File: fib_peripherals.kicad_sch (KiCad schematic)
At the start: 2 parts, among them J1 Raspi_Header, J2 Raspi_Header

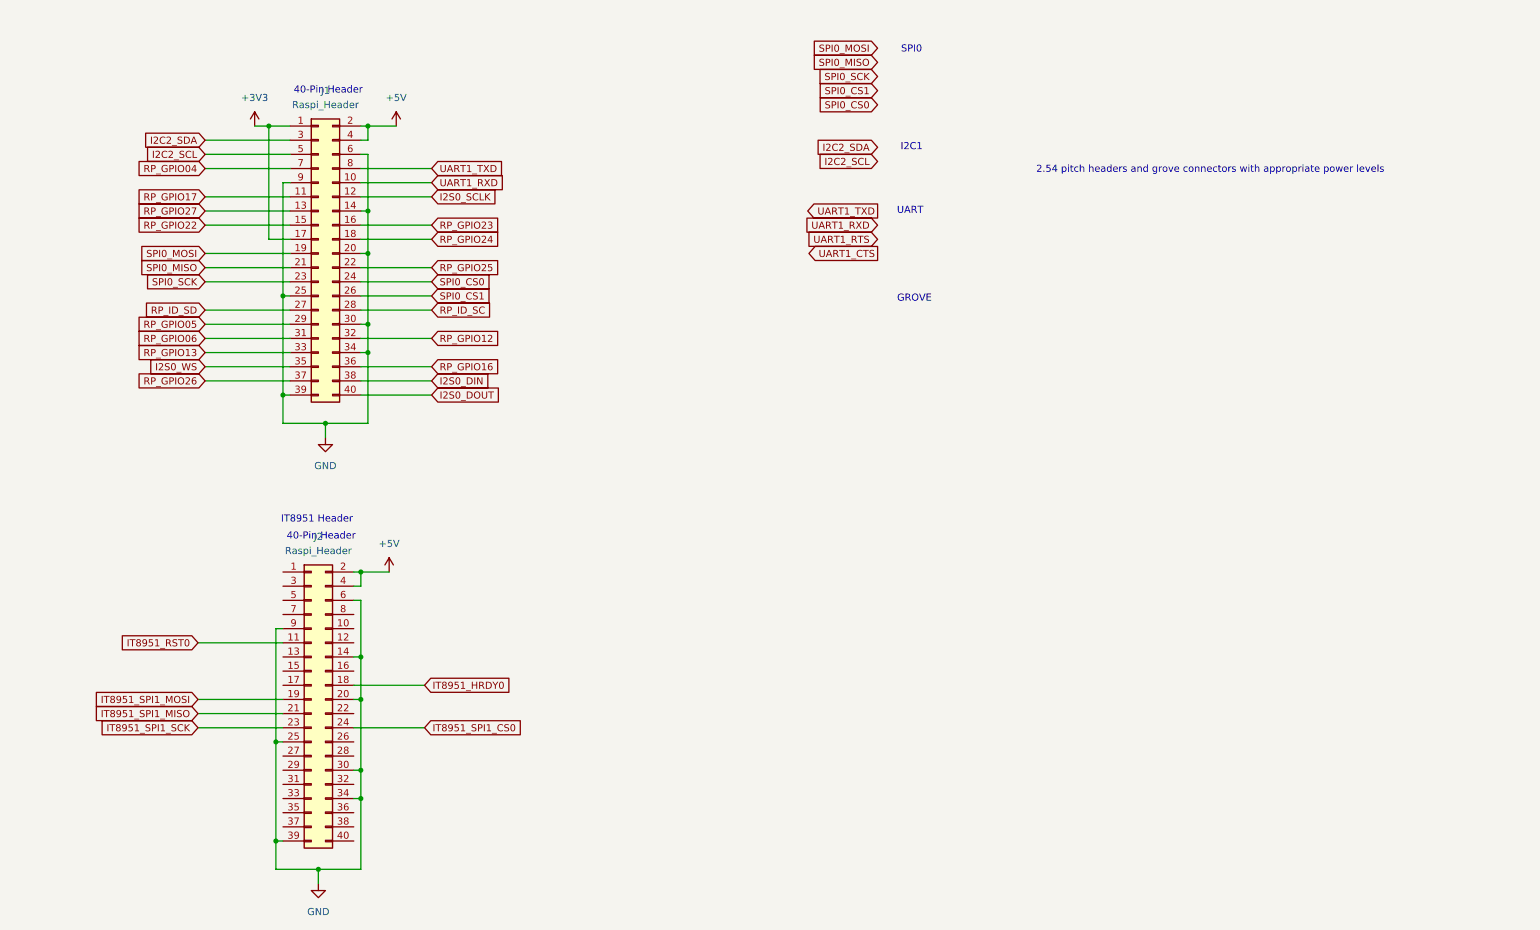
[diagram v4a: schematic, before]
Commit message: added port expander and level shifters, routed peripherals fixed most drc errors, assigned gpios etc.
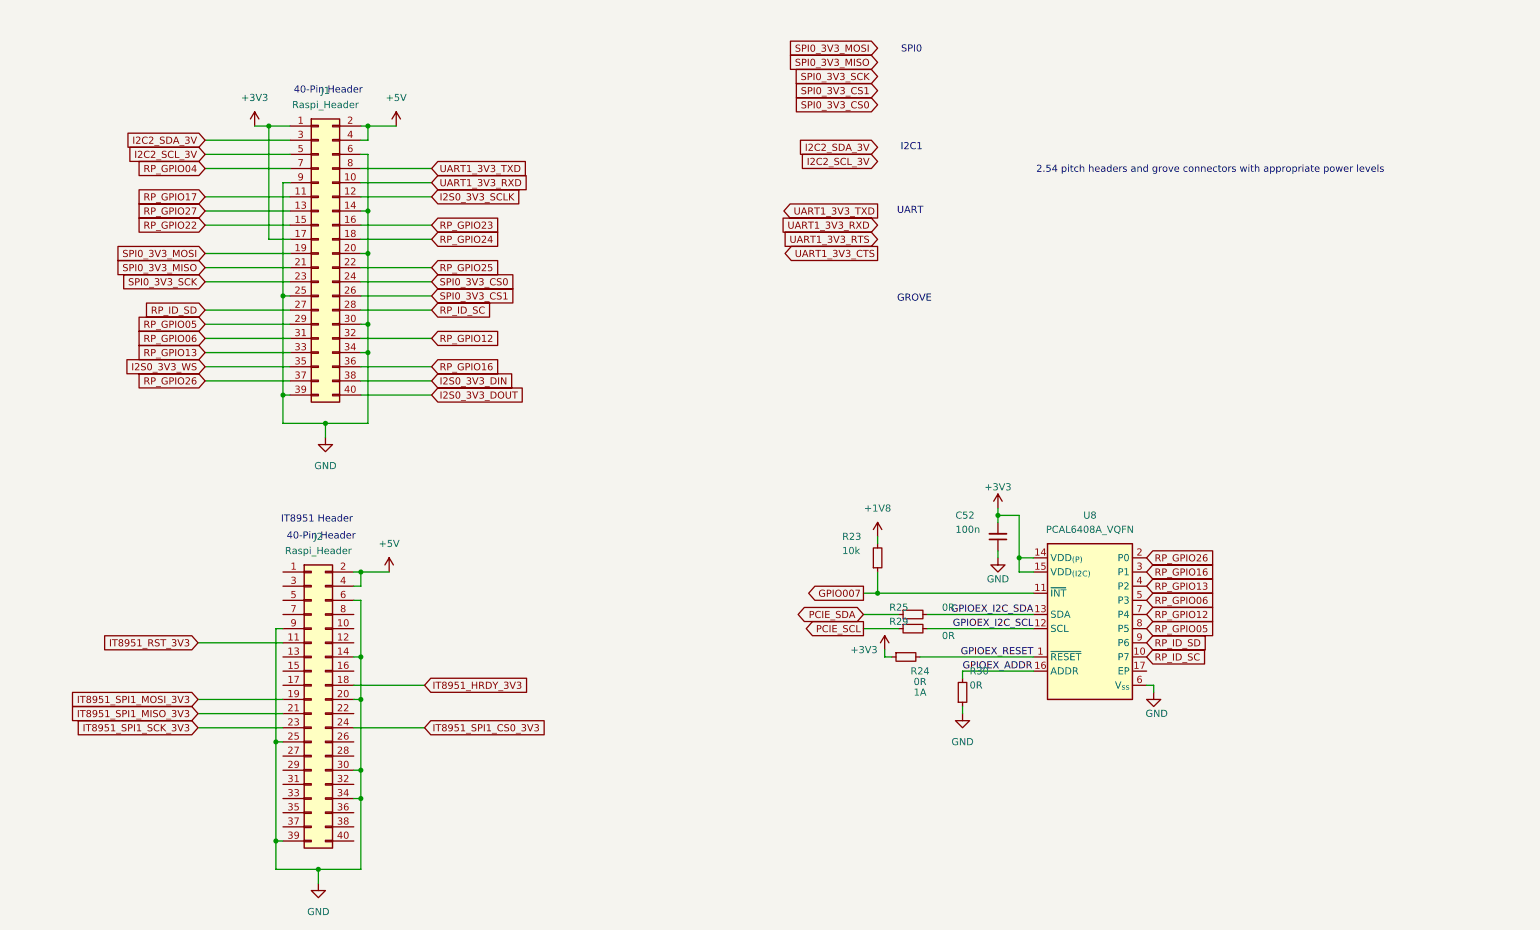
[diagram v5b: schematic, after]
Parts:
- added C52: C_Small_Rota, Capacitor_SMD:C_0402_1005Metric, symbol Fibel2:C_Small_Rota
- added R23, R24, R25, R29, R30: R_Small_Rota, Resistor_SMD:R_0402_1005Metric, symbol Fibel2:R_Small_Rota
- added U8: PCAL6408A_VQFN, Fibel2:QFN50P300X300X100-17N, symbol Fibel2:PCAL6408A_VQFN
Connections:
- net +3V3: now also C52.2, R24.1, U8.14 (VDD_{(P)}), U8.15 (VDD_{(I2C)})
- net GND: now also C52.1, R30.1, U8.6 (V_{ss})
- net RP_GPIO05: now also U8.8 (P5)
- net RP_GPIO06: now also U8.5 (P3)
- net RP_GPIO12: now also U8.7 (P4)
- net RP_GPIO13: now also U8.4 (P2)
- net RP_GPIO16: now also U8.3 (P1)
- net RP_GPIO26: now also U8.2 (P0)
- net RP_ID_SC: now also U8.10 (P7)
- net RP_ID_SD: now also U8.9 (P6)
- net I2C2_SCL renamed I2C2_SCL_3V
- net I2C2_SDA renamed I2C2_SDA_3V
- net I2S0_DIN renamed I2S0_3V3_DIN
- net I2S0_DOUT renamed I2S0_3V3_DOUT
- net I2S0_SCLK renamed I2S0_3V3_SCLK
- net I2S0_WS renamed I2S0_3V3_WS
- net IT8951_HRDY0 renamed IT8951_HRDY_3V3
- net IT8951_RST0 renamed IT8951_RST_3V3
- net IT8951_SPI1_CS0 renamed IT8951_SPI1_CS0_3V3
- net IT8951_SPI1_MISO renamed IT8951_SPI1_MISO_3V3
- net IT8951_SPI1_MOSI renamed IT8951_SPI1_MOSI_3V3
- net IT8951_SPI1_SCK renamed IT8951_SPI1_SCK_3V3
- net SPI0_CS0 renamed SPI0_3V3_CS0
- net SPI0_CS1 renamed SPI0_3V3_CS1
- net SPI0_MISO renamed SPI0_3V3_MISO
- net SPI0_MOSI renamed SPI0_3V3_MOSI
- net SPI0_SCK renamed SPI0_3V3_SCK
- net UART1_RXD renamed UART1_3V3_RXD
- net UART1_TXD renamed UART1_3V3_TXD
- new net +1V8: R23.2
- new net GPIO007: R23.1, U8.11 (~{INT})
- new net GPIOEX_ADDR: R30.2, U8.16 (ADDR)
- new net GPIOEX_I2C_SCL: R29.2, U8.12 (SCL)
- new net GPIOEX_I2C_SDA: R25.2, U8.13 (SDA)
- new net GPIOEX_RESET: R24.2, U8.1 (~{RESET})
- new net PCIE_SCL: R29.1
- new net PCIE_SDA: R25.1

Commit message: routed epd displays, added testpoints and all the little checks and fixe, (regrettably) removed the i80 connector, 99% there, need to double check some things add peripheral connectors, shared-ish storage and vias vias vias
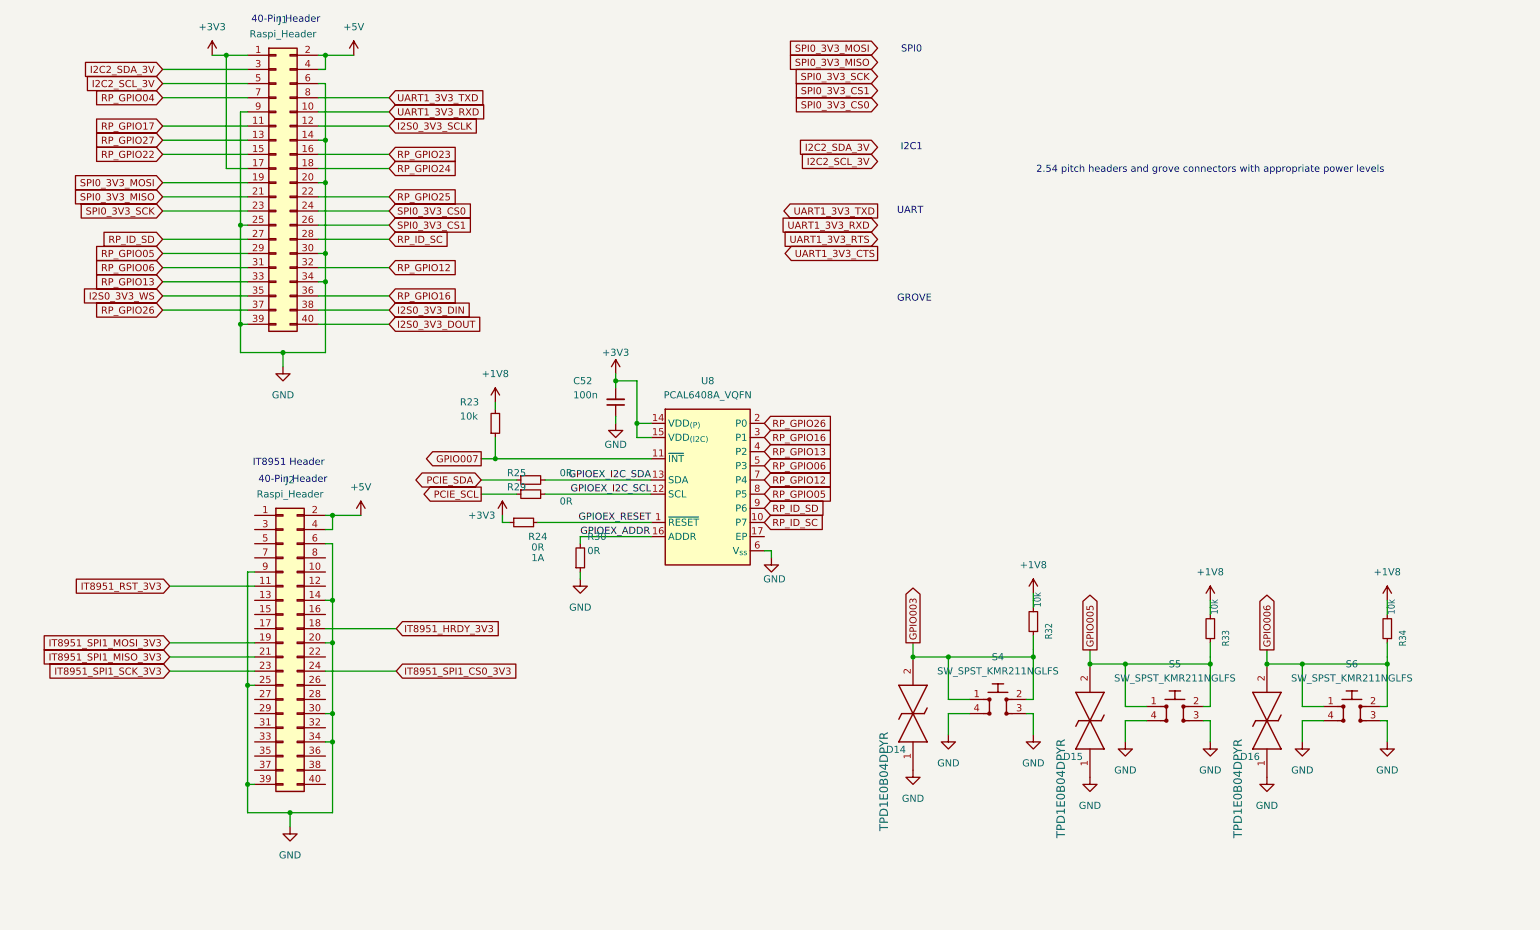
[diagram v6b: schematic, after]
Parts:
- added D14, D15, D16: TPD1E0B04_XDFN-2, Fibel2:TPD1E0B04DPYT, symbol Fibel2:TPD1E0B04DPYT
- added R32, R33, R34: 10k, Resistor_SMD:R_0402_1005Metric, symbol Fibel2:R_Small_Rota
- added S4, S5, S6: SW_SPST_KMR211NGLFS, Fibel2:KMR211NGLFS, symbol Fibel2:SW_KMR211NGLFS_SMD
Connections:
- net +1V8: now also R32.2, R33.2, R34.2
- net GND: now also D14.1, D15.1, D16.1, S4.3, S4.4, S5.3, S5.4, S6.3, S6.4
- new net GPIO003: D14.2, R32.1, S4.1, S4.2
- new net GPIO005: D15.2, R33.1, S5.1, S5.2
- new net GPIO006: D16.2, R34.1, S6.1, S6.2
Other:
- moved on the sheet: C52, J1, J2, R23, R24, R25, R29, R30, U8

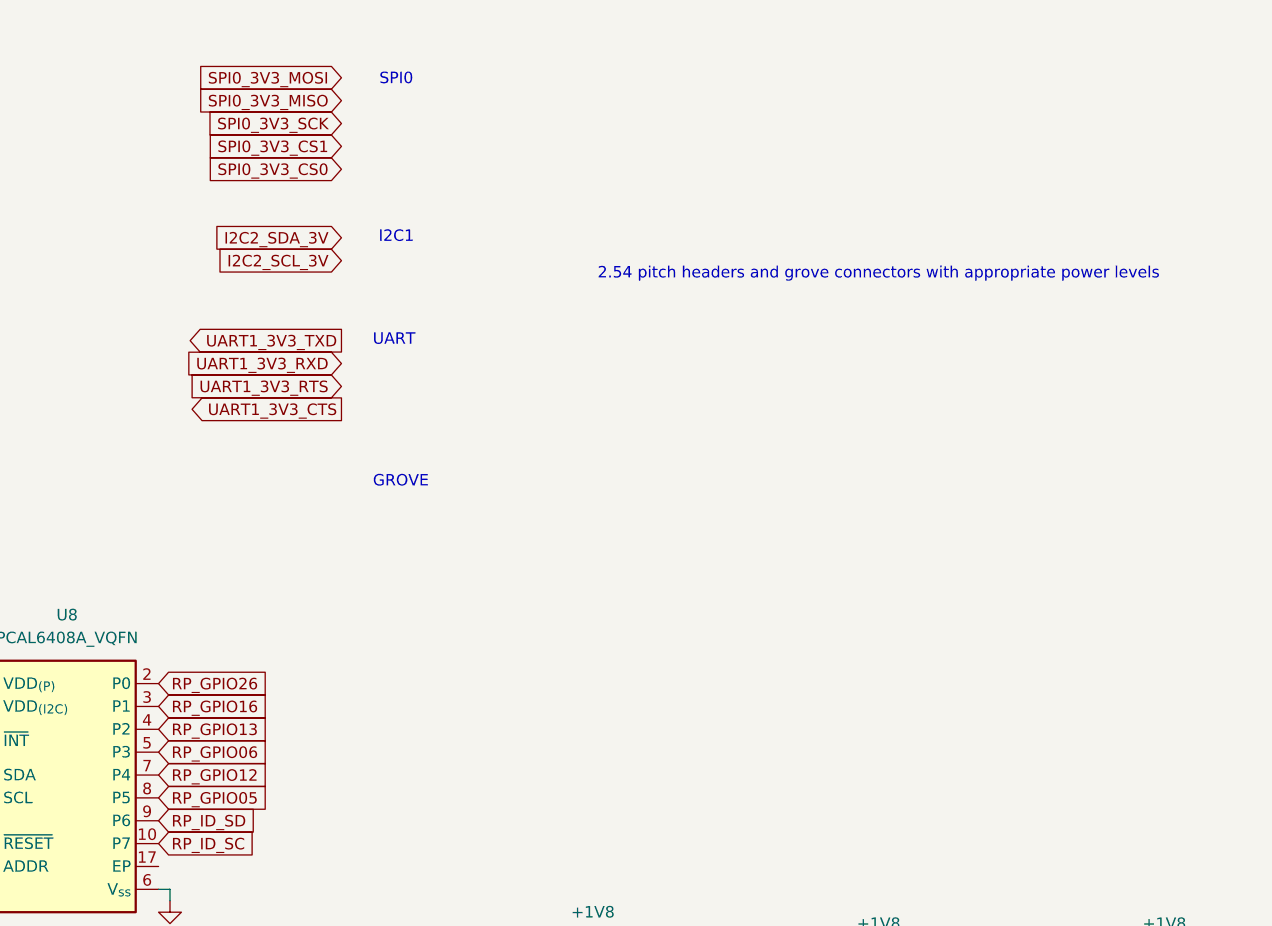
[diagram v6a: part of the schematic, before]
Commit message: finished routing, sanity check and prep fabrication files next
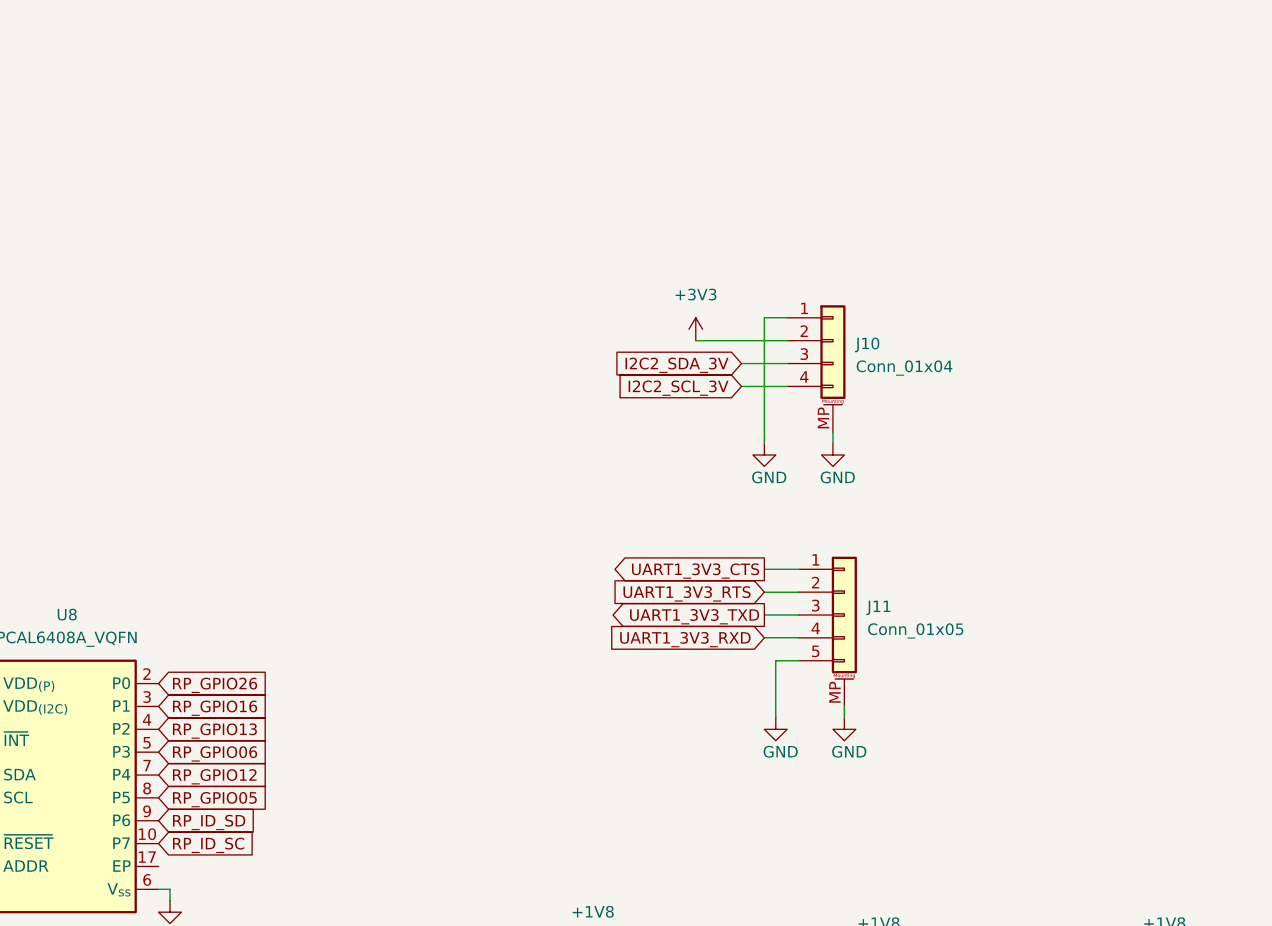
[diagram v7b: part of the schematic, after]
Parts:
- added J10: Conn_01x04, Connector_JST:JST_PH_S4B-PH-SM4-TB_1x04-1MP_P2.00mm_Horizontal, symbol Connector_Generic_MountingPin:Conn_01x04_MountingPin
- added J11: Conn_01x05, Connector_JST:JST_PH_S5B-PH-SM4-TB_1x05-1MP_P2.00mm_Horizontal, symbol Connector_Generic_MountingPin:Conn_01x05_MountingPin
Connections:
- net +3V3: now also J10.2 (Pin_2)
- net GND: now also J10.1 (Pin_1), J10.MP (MountPin), J11.5 (Pin_5), J11.MP (MountPin)
- net I2C2_SCL_3V: now also J10.4 (Pin_4)
- net I2C2_SDA_3V: now also J10.3 (Pin_3)
- net UART1_3V3_CTS: now also J11.1 (Pin_1)
- net UART1_3V3_RTS: now also J11.2 (Pin_2)
- net UART1_3V3_RXD: now also J11.4 (Pin_4)
- net UART1_3V3_TXD: now also J11.3 (Pin_3)
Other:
- note removed: "2.54 pitch headers and grove connectors with appropriate power levels"
- note removed: "GROVE"
- note removed: "I2C1"
- note removed: "SPI0"
- note removed: "UART"

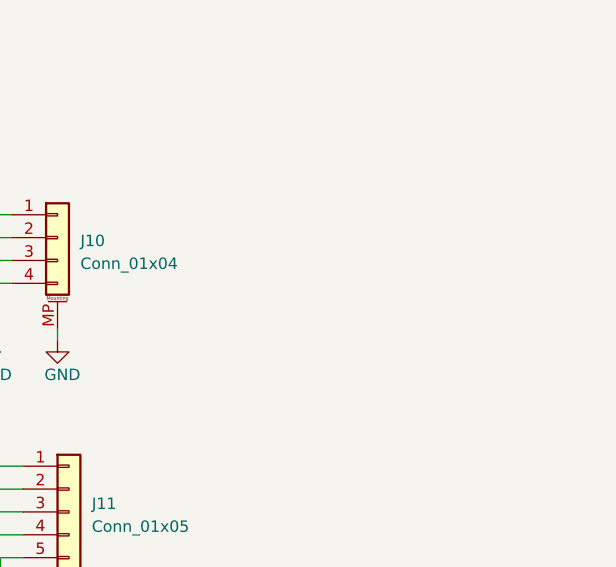
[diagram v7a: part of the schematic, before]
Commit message: added second i2c, modified 40 pin headers
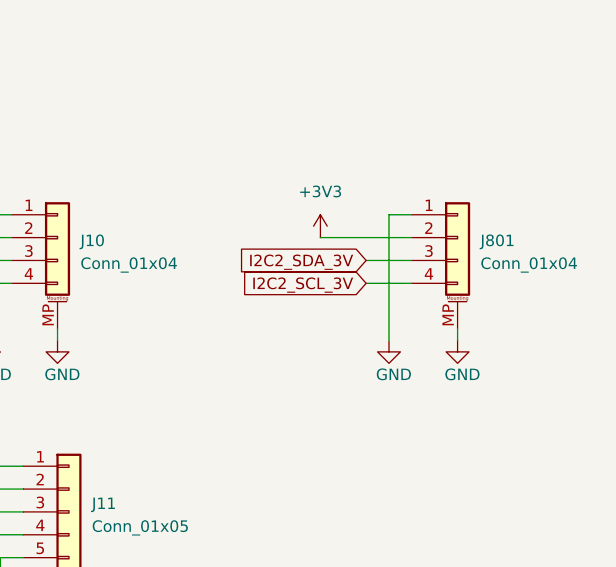
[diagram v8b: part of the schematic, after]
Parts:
- added J801: Conn_01x04, Connector_JST:JST_PH_S4B-PH-SM4-TB_1x04-1MP_P2.00mm_Horizontal, symbol Connector_Generic_MountingPin:Conn_01x04_MountingPin
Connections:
- net +3V3: now also J801.2 (Pin_2)
- net GND: now also J801.1 (Pin_1), J801.MP (MountPin)
- net I2C2_SCL_3V: now also J801.4 (Pin_4)
- net I2C2_SDA_3V: now also J801.3 (Pin_3)
